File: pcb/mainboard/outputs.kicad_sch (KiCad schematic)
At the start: 71 parts, among them U38 ISL24021IRT065Z-T7A‎, U39 ISL24021IRT065Z-T7A‎, U40 ISL24021IRT065Z-T7A‎, U41 ISL24021IRT065Z-T7A‎, U42 DAC60508, U43 ISL24021IRT065Z-T7A‎, U44 ISL24021IRT065Z-T7A‎, U45 ISL24021IRT065Z-T7A‎, U46 ISL24021IRT065Z-T7A‎, U47 74LVC1T45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

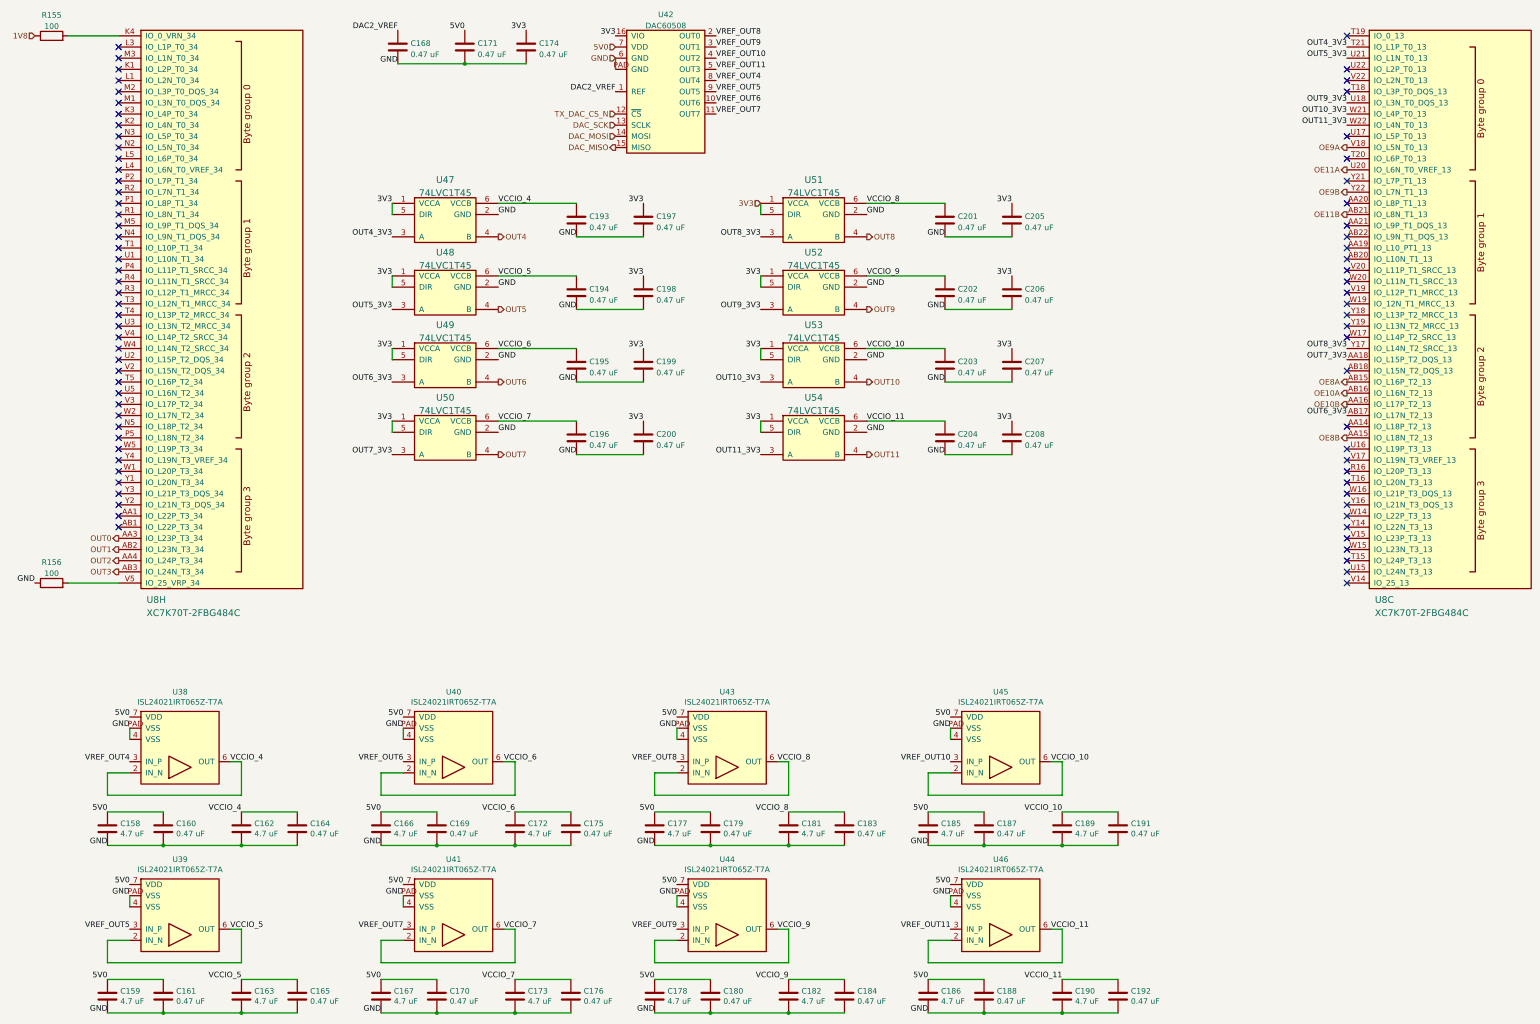
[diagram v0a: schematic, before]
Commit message: Tweaks to debug connectors, hooked up TX DAC
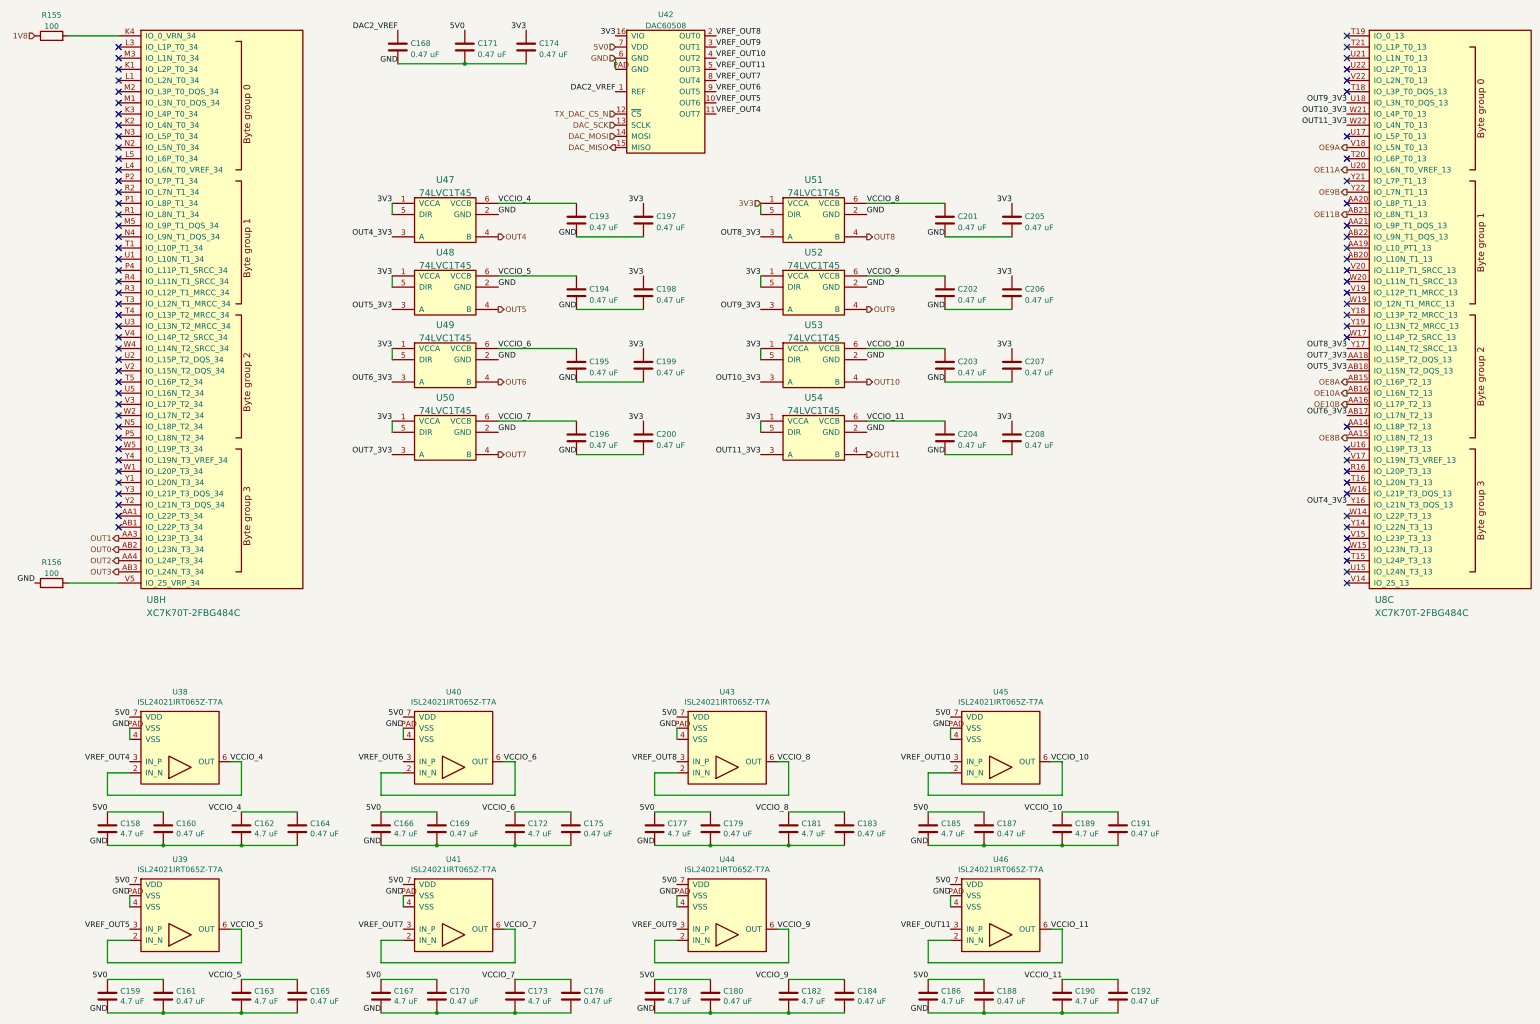
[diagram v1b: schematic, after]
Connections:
- net OUT0: now also U8.AB2 (IO_L23N_T3_34); no longer U8.AA3 (IO_L23P_T3_34)
- net OUT1: now also U8.AA3 (IO_L23P_T3_34); no longer U8.AB2 (IO_L23N_T3_34)
- net OUT4_3V3: now also U8.Y16 (IO_L21N_T3_DQS_13); no longer U8.T21 (IO_L1P_T0_13)
- net OUT5_3V3: now also U8.AB18 (IO_L15N_T2_DQS_13); no longer U8.U21 (IO_L1N_T0_13)
- net VREF_OUT4: now also U42.11 (OUT7); no longer U42.8 (OUT4)
- net VREF_OUT5: now also U42.10 (OUT6); no longer U42.9 (OUT5)
- net VREF_OUT6: now also U42.9 (OUT5); no longer U42.10 (OUT6)
- net VREF_OUT7: now also U42.8 (OUT4); no longer U42.11 (OUT7)
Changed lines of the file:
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@@
   (no_connect (at 349.25 95.25))
   (no_connect (at 349.25 148.59))
+  (no_connect (at 349.25 31.75))
   (no_connect (at 349.25 92.71))
   (no_connect (at 69.85 135.89))
@@
   (no_connect (at 69.85 100.33))
   (no_connect (at 349.25 74.93))
-  (no_connect (at 349.25 102.87))
   (no_connect (at 349.25 54.61))
   (no_connect (at 69.85 31.75))
@@
   (no_connect (at 69.85 39.37))
   (no_connect (at 69.85 123.19))
-  (no_connect (at 349.25 133.35))
   (no_connect (at 69.85 44.45))
   (no_connect (at 349.25 123.19))
@@
   (no_connect (at 69.85 64.77))
   (no_connect (at 349.25 128.27))
+  (no_connect (at 349.25 29.21))
   (no_connect (at 349.25 130.81))
   (no_connect (at 69.85 95.25))
@@
     (effects (font (size 1.27 1.27)) (justify left bottom))
   )
-  (label "VREF_OUT5" (at 205.74 39.37 0)
+  (label "VREF_OUT5" (at 205.74 41.91 0)
     (effects (font (size 1.27 1.27)) (justify left bottom))
   )
@@
     (effects (font (size 1.27 1.27)) (justify right bottom))
   )
-  (label "OUT4_3V3" (at 349.25 29.21 180)
+  (label "OUT4_3V3" (at 349.25 133.35 180)
     (effects (font (size 1.27 1.27)) (justify right bottom))
   )
@@
     (effects (font (size 1.27 1.27)) (justify right bottom))
   )
-  (label "VREF_OUT6" (at 205.74 41.91 0)
+  (label "VREF_OUT6" (at 205.74 39.37 0)
     (effects (font (size 1.27 1.27)) (justify left bottom))
   )
@@
     (effects (font (size 1.27 1.27)) (justify left bottom))
   )
-  (label "OUT5_3V3" (at 349.25 31.75 180)
+  (label "OUT5_3V3" (at 349.25 102.87 180)
     (effects (font (size 1.27 1.27)) (justify right bottom))
   )
@@
     (effects (font (size 1.27 1.27)) (justify left bottom))
   )
-  (label "VREF_OUT7" (at 205.74 44.45 0)
+  (label "VREF_OUT7" (at 205.74 36.83 0)
     (effects (font (size 1.27 1.27)) (justify left bottom))
   )
@@
     (effects (font (size 1.27 1.27)) (justify left bottom))
   )
-  (label "VREF_OUT4" (at 205.74 36.83 0)
+  (label "VREF_OUT4" (at 205.74 44.45 0)
     (effects (font (size 1.27 1.27)) (justify left bottom))
   )
@@
     (effects (font (size 1.27 1.27)) (justify right))
   )
-  (hierarchical_label "OUT1" (shape output) (at 69.85 143.51 180)
+  (hierarchical_label "OUT1" (shape output) (at 69.85 140.97 180)
     (effects (font (size 1.27 1.27)) (justify right))
   )
@@
     (effects (font (size 1.27 1.27)) (justify right))
   )
-  (hierarchical_label "OUT0" (shape output) (at 69.85 140.97 180)
-    (effects (font (size 1.27 1.27)) (justify right))
-  )
+  (hierarchical_label "OUT0" (shape output) (at 69.85 143.51 180)
+    (effects (font (size 1.27 1.27)) (justify right))
+  )

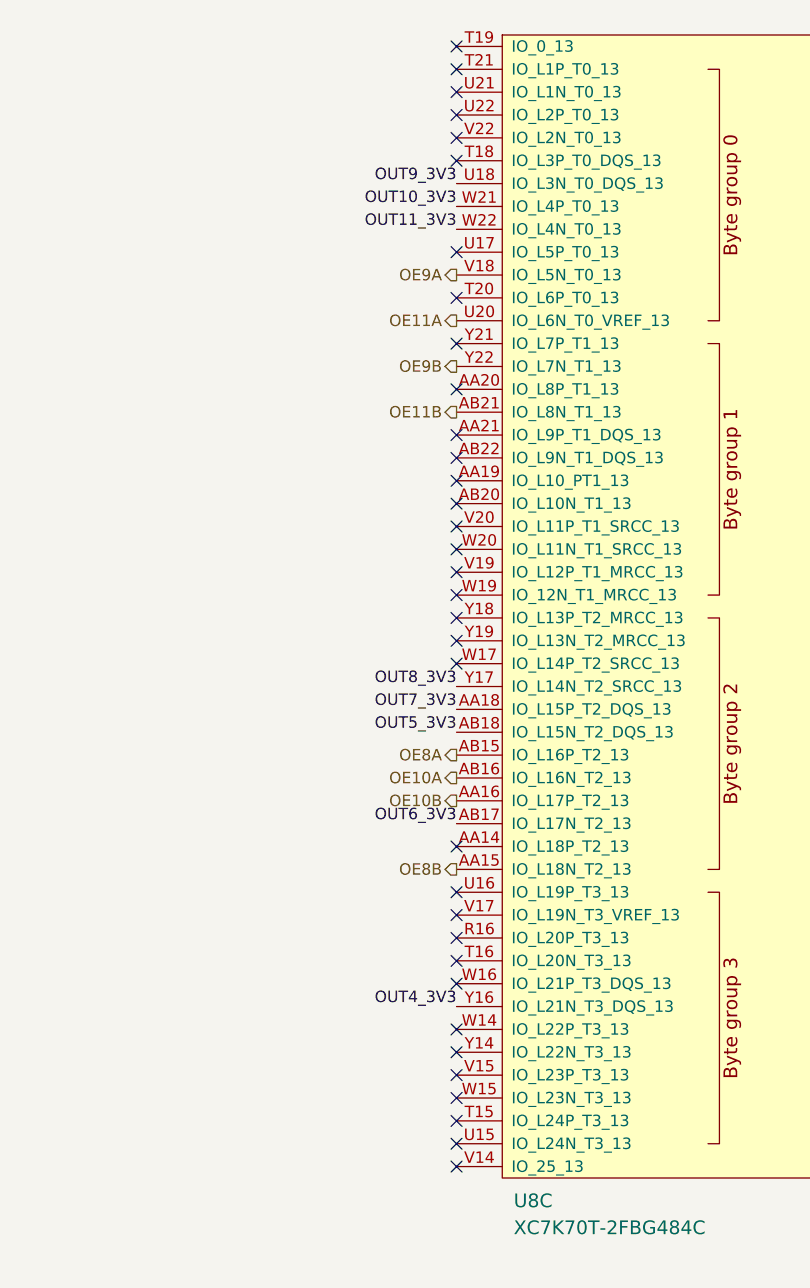
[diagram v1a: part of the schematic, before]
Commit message: Hooked up soft power/reset buttons
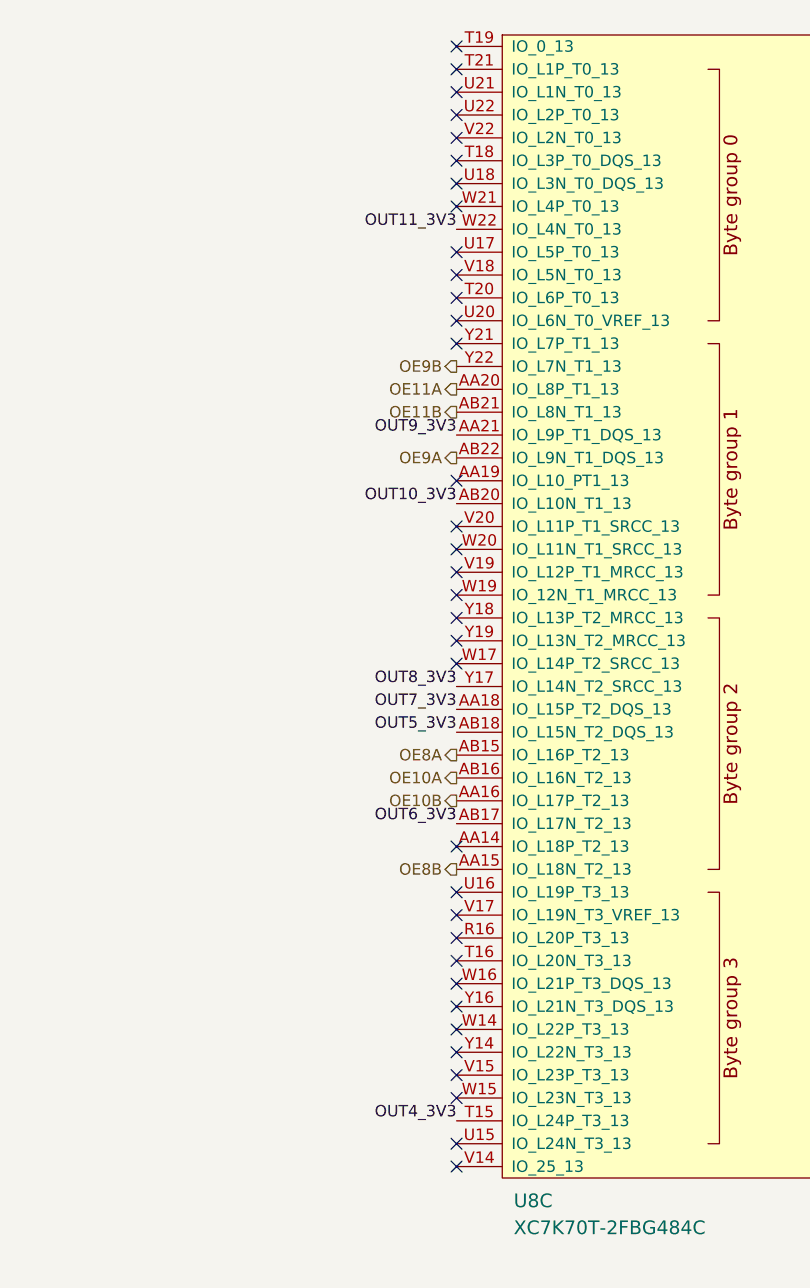
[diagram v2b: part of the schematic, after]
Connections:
- net OE11A: now also U8.AA20 (IO_L8P_T1_13); no longer U8.U20 (IO_L6N_T0_VREF_13)
- net OE9A: now also U8.AB22 (IO_L9N_T1_DQS_13); no longer U8.V18 (IO_L5N_T0_13)
- net OUT10_3V3: now also U8.AB20 (IO_L10N_T1_13); no longer U8.W21 (IO_L4P_T0_13)
- net OUT4_3V3: now also U8.T15 (IO_L24P_T3_13); no longer U8.Y16 (IO_L21N_T3_DQS_13)
- net OUT9_3V3: now also U8.AA21 (IO_L9P_T1_DQS_13); no longer U8.U18 (IO_L3N_T0_DQS_13)
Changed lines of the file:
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@@
   (no_connect (at 349.25 36.83))
   (no_connect (at 349.25 138.43))
+  (no_connect (at 349.25 44.45))
   (no_connect (at 69.85 74.93))
   (no_connect (at 349.25 39.37))
@@
   (no_connect (at 69.85 135.89))
   (no_connect (at 69.85 128.27))
+  (no_connect (at 349.25 133.35))
   (no_connect (at 69.85 130.81))
   (no_connect (at 69.85 80.01))
@@
   (no_connect (at 69.85 87.63))
   (no_connect (at 69.85 69.85))
+  (no_connect (at 349.25 52.07))
   (no_connect (at 69.85 67.31))
   (no_connect (at 69.85 115.57))
@@
   (no_connect (at 349.25 49.53))
   (no_connect (at 69.85 77.47))
-  (no_connect (at 349.25 77.47))
+  (no_connect (at 349.25 41.91))
   (no_connect (at 349.25 90.17))
+  (no_connect (at 349.25 57.15))
   (no_connect (at 69.85 125.73))
   (no_connect (at 69.85 52.07))
@@
   (no_connect (at 69.85 54.61))
   (no_connect (at 69.85 57.15))
-  (no_connect (at 349.25 72.39))
   (no_connect (at 69.85 72.39))
   (no_connect (at 349.25 143.51))
@@
   (no_connect (at 349.25 85.09))
   (no_connect (at 349.25 115.57))
-  (no_connect (at 349.25 69.85))
   (no_connect (at 349.25 135.89))
-  (no_connect (at 349.25 146.05))
   (no_connect (at 69.85 110.49))
-  (no_connect (at 349.25 64.77))
   (no_connect (at 349.25 120.65))
   (no_connect (at 69.85 105.41))
@@
     (effects (font (size 1.27 1.27)) (justify right bottom))
   )
-  (label "OUT9_3V3" (at 349.25 41.91 180)
+  (label "OUT9_3V3" (at 349.25 69.85 180)
     (effects (font (size 1.27 1.27)) (justify right bottom))
   )
@@
     (effects (font (size 1.27 1.27)) (justify right bottom))
   )
-  (label "OUT4_3V3" (at 349.25 133.35 180)
+  (label "OUT4_3V3" (at 349.25 146.05 180)
     (effects (font (size 1.27 1.27)) (justify right bottom))
   )
@@
     (effects (font (size 1.27 1.27)) (justify right bottom))
   )
-  (label "OUT10_3V3" (at 349.25 44.45 180)
+  (label "OUT10_3V3" (at 349.25 77.47 180)
     (effects (font (size 1.27 1.27)) (justify right bottom))
   )
@@
     (effects (font (size 1.27 1.27)) (justify left))
   )
-  (hierarchical_label "OE9A" (shape output) (at 349.25 52.07 180)
+  (hierarchical_label "OE9A" (shape output) (at 349.25 72.39 180)
     (effects (font (size 1.27 1.27)) (justify right))
   )
@@
     (effects (font (size 1.27 1.27)) (justify left))
   )
-  (hierarchical_label "OE11A" (shape output) (at 349.25 57.15 180)
-    (effects (font (size 1.27 1.27)) (justify right))
-  )
+  (hierarchical_label "OE11A" (shape output) (at 349.25 64.77 180)
+    (effects (font (size 1.27 1.27)) (justify right))
+  )
